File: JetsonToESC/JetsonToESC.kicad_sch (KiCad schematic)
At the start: 1 part, among them U1 ESP32-C3_SUPERMINI_TH

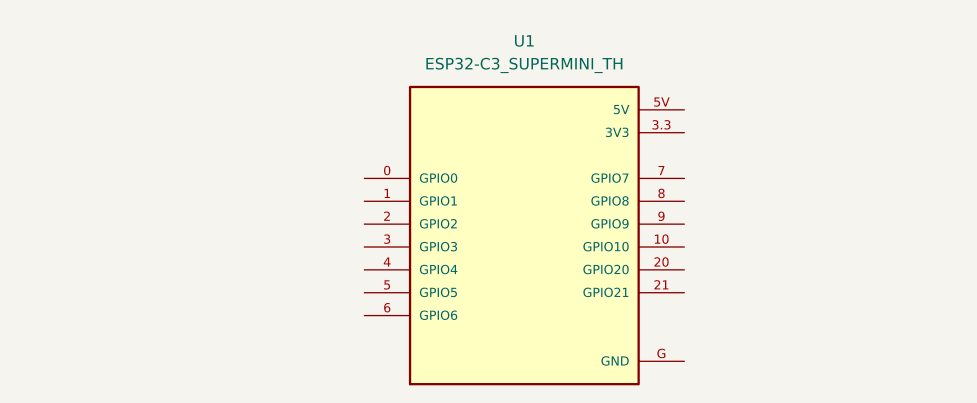
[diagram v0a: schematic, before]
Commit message: Added footprints, connectors and cutout
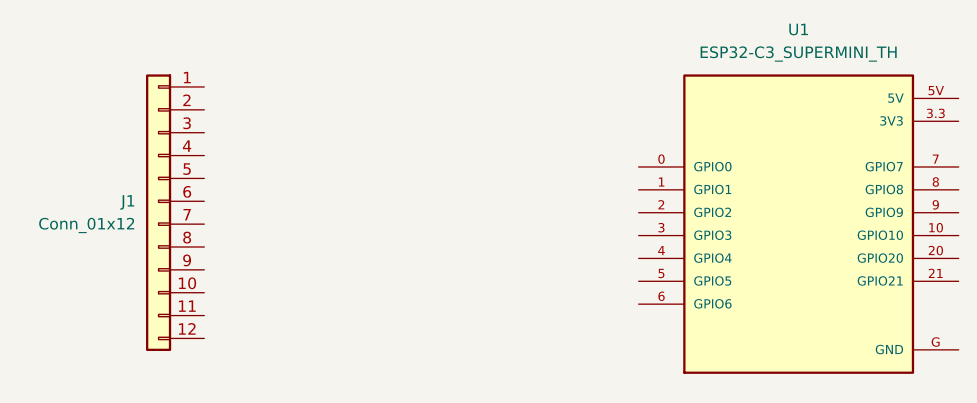
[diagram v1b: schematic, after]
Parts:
- added J1: Conn_01x12, Connector_PinSocket_2.54mm:PinSocket_1x12_P2.54mm_Horizontal, symbol Connector_Generic:Conn_01x12
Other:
- moved on the sheet: U1
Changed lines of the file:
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@@
 	(symbol
 		(lib_id "ESP32-C3_SUPERMINI_TH:ESP32-C3_SUPERMINI_TH")
-		(at 124.46 88.9 0)
+		(at 154.94 87.63 0)
 		(unit 1)
 		(exclude_from_sim no)
@@
 		(fields_autoplaced yes)
 		(property "Reference" "U1"
-			(at 124.46 68.58 0)
+			(at 154.94 67.31 0)
 			(effects
 				(font
@@
 		)
 		(property "Value" "ESP32-C3_SUPERMINI_TH"
-			(at 124.46 71.12 0)
+			(at 154.94 69.85 0)
 			(effects
 				(font
@@
 		)
 		(property "Footprint" "ESP32ModulesLibrary:MODULE_ESP32-C3_SUPERMINI_TH"
-			(at 124.46 88.9 0)
+			(at 154.94 87.63 0)
 			(effects
 				(font
@@
 		)
 		(property "Datasheet" ""
-			(at 124.46 88.9 0)
+			(at 154.94 87.63 0)
 			(effects
 				(font
@@
 		)
 		(property "Description" ""
-			(at 124.46 88.9 0)
+			(at 154.94 87.63 0)
 			(effects
 				(font
@@
 		)
 		(property "MF" "Espressif Systems"
-			(at 124.46 88.9 0)
+			(at 154.94 87.63 0)
 			(effects
 				(font
@@
 		)
 		(property "Description_1" "\n                        \n                            Super tiny ESP32-C3 board\n                        \n"
-			(at 124.46 88.9 0)
+			(at 154.94 87.63 0)
 			(effects
 				(font
@@
 		)
 		(property "CREATOR" "DIZAR"
-			(at 124.46 88.9 0)
+			(at 154.94 87.63 0)
 			(effects
 				(font
@@
 		)
 		(property "Price" "None"
-			(at 124.46 88.9 0)
+			(at 154.94 87.63 0)
 			(effects
 				(font
@@
 		)
 		(property "Package" "Package"
-			(at 124.46 88.9 0)
+			(at 154.94 87.63 0)
 			(effects
 				(font
@@
 		)
 		(property "Check_prices" "https://www.snapeda.com/parts/ESP32-C3%20SuperMini_TH/Espressif+Systems/view-part/?ref=eda"
-			(at 124.46 88.9 0)
+			(at 154.94 87.63 0)
 			(effects
 				(font
@@
 		)
 		(property "STANDARD" "IPC-7351B"
-			(at 124.46 88.9 0)
+			(at 154.94 87.63 0)
 			(effects
 				(font
@@
 		)
 		(property "VERIFIER" ""
-			(at 124.46 88.9 0)
+			(at 154.94 87.63 0)
 			(effects
 				(font
@@
 		)
 		(property "SnapEDA_Link" "https://www.snapeda.com/parts/ESP32-C3%20SuperMini_TH/Espressif+Systems/view-part/?ref=snap"
-			(at 124.46 88.9 0)
+			(at 154.94 87.63 0)
 			(effects
 				(font
@@
 		)
 		(property "MP" "ESP32-C3 SuperMini_TH"
-			(at 124.46 88.9 0)
+			(at 154.94 87.63 0)
 			(effects
 				(font
@@
 		)
 		(property "Availability" "Not in stock"
-			(at 124.46 88.9 0)
+			(at 154.94 87.63 0)
 			(effects
 				(font
@@
 		)
 		(property "MANUFACTURER" "Espressif Systems"
-			(at 124.46 88.9 0)
+			(at 154.94 87.63 0)
 			(effects
 				(font
@@
 					(unit 1)
 				)
+			)
+		)
+	)
+	(symbol
+		(lib_id "Connector_Generic:Conn_01x12")
+		(at 83.82 86.36 0)
+		(mirror y)
+		(unit 1)
+		(exclude_from_sim no)
+		(in_bom yes)
+		(on_board yes)
+		(dnp no)
+		(property "Reference" "J1"
+			(at 81.28 86.3599 0)
+			(effects
+				(font
+					(size 1.27 1.27)
+				)
+				(justify left)
+			)
+		)
+		(property "Value" "Conn_01x12"
+			(at 81.28 88.8999 0)
+			(effects
+				(font
+					(size 1.27 1.27)
+				)
+				(justify left)
+			)
+		)
+		(property "Footprint" "Connector_PinSocket_2.54mm:PinSocket_1x12_P2.54mm_Horizontal"
+			(at 83.82 86.36 0)
+			(effects
+				(font
+					(size 1.27 1.27)
+				)
+				(hide yes)
+			)
+		)
+		(property "Datasheet" "~"
+			(at 83.82 86.36 0)
+			(effects
+				(font
+					(size 1.27 1.27)
+				)
+				(hide yes)
+			)
+		)
+		(property "Description" "Generic connector, single row, 01x12, script generated (kicad-library-utils/schlib/autogen/connector/)"
+			(at 83.82 86.36 0)
+			(effects
+				(font
+					(size 1.27 1.27)
+				)
+				(hide yes)
+			)
+		)
+		(pin "10"
+		)
+		(pin "3"
+		)
+		(pin "1"
+		)
+		(pin "5"
+		)
+		(pin "12"
+		)
+		(pin "2"
+		)
+		(pin "7"
+		)
+		(pin "11"
+		)
+		(pin "4"
+		)
+		(pin "6"
+		)
+		(pin "9"
+		)
+		(pin "8"
+		)
+		(instances
+			(project ""
+				(path "/47af999a-55f7-4333-ac4c-b272b7fb2895"
+					(reference "J1")
+					(unit 1)
+				)

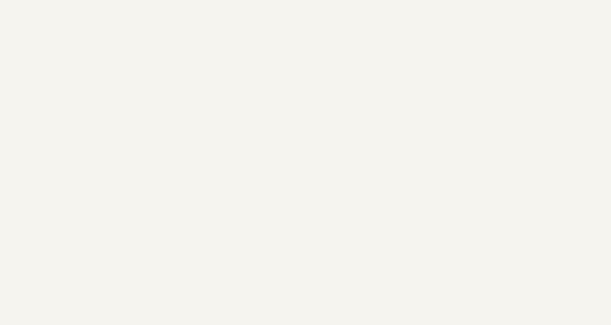
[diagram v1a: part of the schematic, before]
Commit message: Added mechanic drills
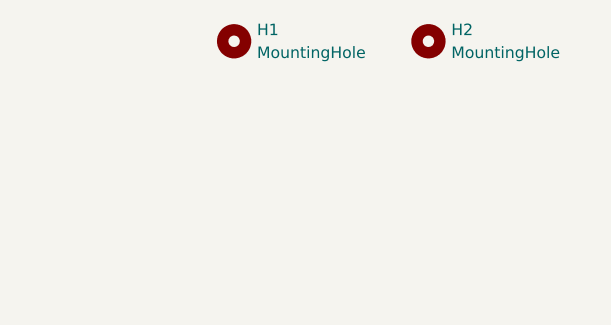
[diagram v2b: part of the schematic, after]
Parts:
- added H1, H2: MountingHole, TestPoint:TestPoint_Plated_Hole_D3.0mm, symbol Mechanical:MountingHole
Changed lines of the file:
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@@
 	(paper "A4")
+	(symbol
+		(lib_id "Mechanical:MountingHole")
+		(at 148.59 25.4 0)
+		(unit 1)
+		(exclude_from_sim yes)
+		(in_bom no)
+		(on_board yes)
+		(dnp no)
+		(fields_autoplaced yes)
+		(property "Reference" "H1"
+			(at 151.13 24.1299 0)
+			(effects
+				(font
+					(size 1.27 1.27)
+				)
+				(justify left)
+			)
+		)
+		(property "Value" "MountingHole"
+			(at 151.13 26.6699 0)
+			(effects
+				(font
+					(size 1.27 1.27)
+				)
+				(justify left)
+			)
+		)
+		(property "Footprint" "TestPoint:TestPoint_Plated_Hole_D3.0mm"
+			(at 148.59 25.4 0)
+			(effects
+				(font
+					(size 1.27 1.27)
+				)
+				(hide yes)
+			)
+		)
+		(property "Datasheet" "~"
+			(at 148.59 25.4 0)
+			(effects
+				(font
+					(size 1.27 1.27)
+				)
+				(hide yes)
+			)
+		)
+		(property "Description" "Mounting Hole without connection"
+			(at 148.59 25.4 0)
+			(effects
+				(font
+					(size 1.27 1.27)
+				)
+				(hide yes)
+			)
+		)
+		(instances
+			(project ""
+				(path "/47af999a-55f7-4333-ac4c-b272b7fb2895"
+					(reference "H1")
+					(unit 1)
+				)
+			)
+		)
+	)
 	(symbol
 		(lib_id "ESP32-C3_SUPERMINI_TH:ESP32-C3_SUPERMINI_TH")
@@
 					(unit 1)
 				)
+			)
+		)
+	)
+	(symbol
+		(lib_id "Mechanical:MountingHole")
+		(at 170.18 25.4 0)
+		(unit 1)
+		(exclude_from_sim yes)
+		(in_bom no)
+		(on_board yes)
+		(dnp no)
+		(fields_autoplaced yes)
+		(property "Reference" "H2"
+			(at 172.72 24.1299 0)
+			(effects
+				(font
+					(size 1.27 1.27)
+				)
+				(justify left)
+			)
+		)
+		(property "Value" "MountingHole"
+			(at 172.72 26.6699 0)
+			(effects
+				(font
+					(size 1.27 1.27)
+				)
+				(justify left)
+			)
+		)
+		(property "Footprint" "TestPoint:TestPoint_Plated_Hole_D3.0mm"
+			(at 170.18 25.4 0)
+			(effects
+				(font
+					(size 1.27 1.27)
+				)
+				(hide yes)
+			)
+		)
+		(property "Datasheet" "~"
+			(at 170.18 25.4 0)
+			(effects
+				(font
+					(size 1.27 1.27)
+				)
+				(hide yes)
+			)
+		)
+		(property "Description" "Mounting Hole without connection"
+			(at 170.18 25.4 0)
+			(effects
+				(font
+					(size 1.27 1.27)
+				)
+				(hide yes)
+			)
+		)
+		(instances
+			(project "JetsonToESC"
+				(path "/47af999a-55f7-4333-ac4c-b272b7fb2895"
+					(reference "H2")
+					(unit 1)
+				)

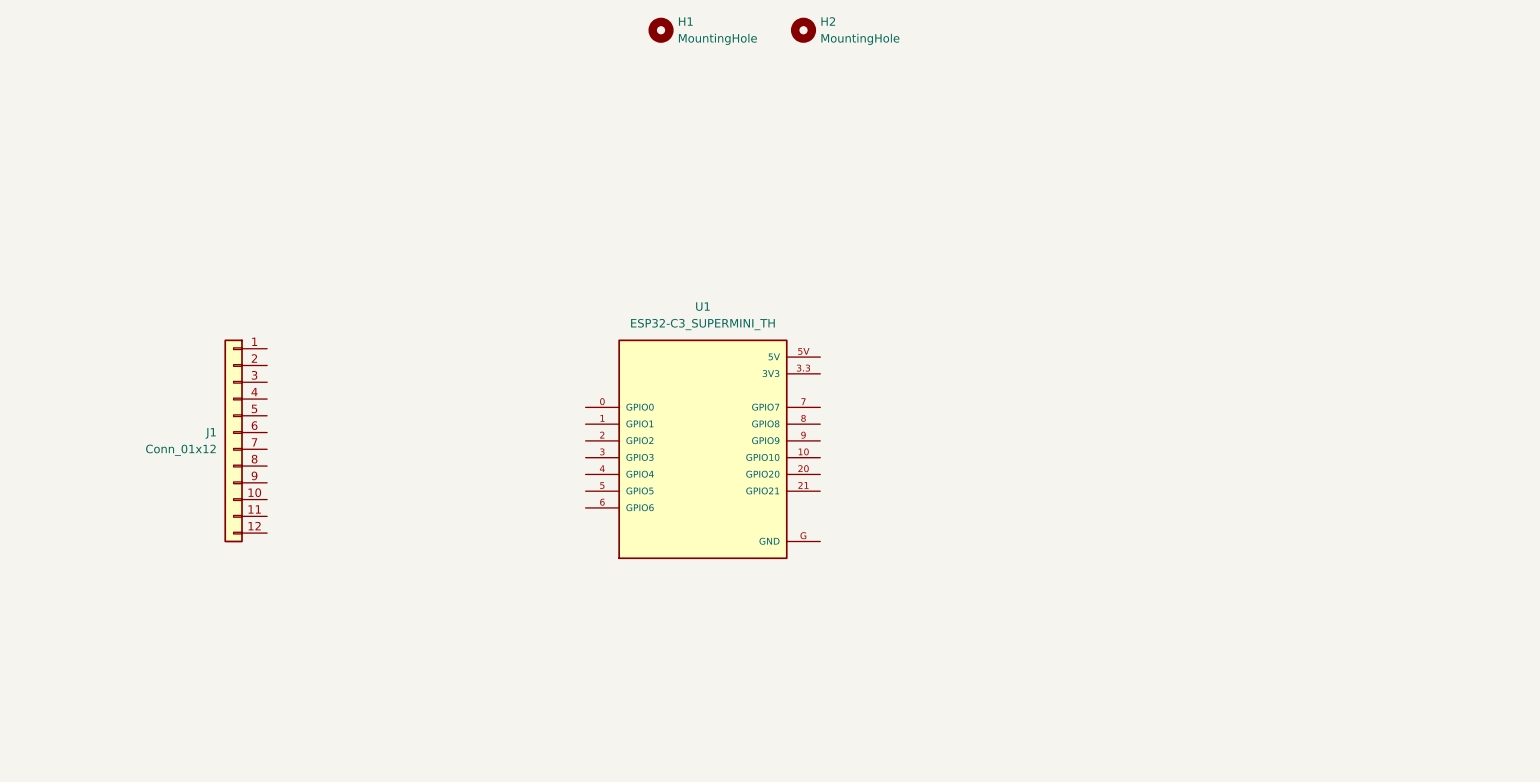
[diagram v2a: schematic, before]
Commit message: Added most of components and preliminar routing
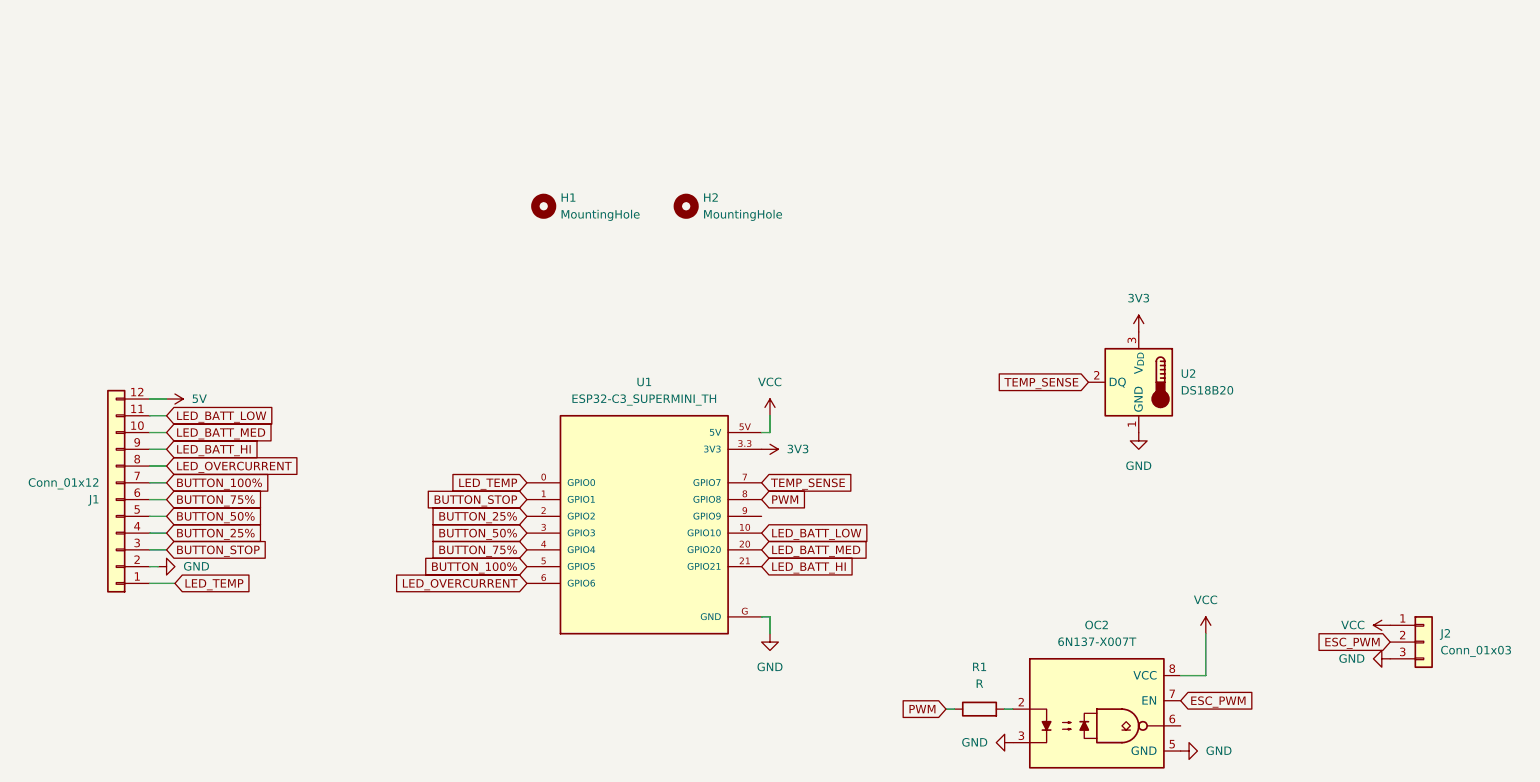
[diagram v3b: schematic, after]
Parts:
- added J2: Conn_01x03, Connector_JST:JST_EH_B3B-EH-A_1x03_P2.50mm_Vertical, symbol Connector_Generic:Conn_01x03
- added OC2: 6N137-X007T, PCM_Package_DIP_AKL:SMDIP-8_W9.53mm, symbol PCM_Optocoupler_Logic_AKL:6N137-X007T
- added R1: R, PCM_Resistor_SMD_AKL:R_0603_1608Metric, symbol Device:R
- added U2: DS18B20, Package_TO_SOT_THT:TO-92_Inline, symbol Sensor_Temperature:DS18B20
- H1, H2: footprint TestPoint:TestPoint_Plated_Hole_D3.0mm -> TestPoint:TestPoint_Plated_Hole_D2.0mm
- J1: footprint Connector_PinSocket_2.54mm:PinSocket_1x12_P2.54mm_Horizontal -> Connector_JST:JST_EH_S12B-EH_1x12_P2.50mm_Horizontal
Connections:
- net LED_TEMP: now reaches U1.0 (GPIO0)
- net LED_TEMP: now also J1.1 (Pin_1)
- net BUTTON_STOP: now reaches U1.1 (GPIO1)
- net BUTTON_STOP: now also J1.3 (Pin_3)
- net LED_BATT_LOW: now reaches U1.10 (GPIO10)
- net LED_BATT_LOW: now also J1.11 (Pin_11)
- net BUTTON_25%: now reaches U1.2 (GPIO2)
- net BUTTON_25%: now also J1.4 (Pin_4)
- net LED_BATT_MED: now reaches U1.20 (GPIO20)
- net LED_BATT_MED: now also J1.10 (Pin_10)
- net LED_BATT_HI: now reaches U1.21 (GPIO21)
- net LED_BATT_HI: now also J1.9 (Pin_9)
- net BUTTON_50%: now reaches U1.3 (GPIO3)
- net BUTTON_50%: now also J1.5 (Pin_5)
- net 3V3: now reaches U1.3.3 (3V3)
- net 3V3: now also U2.3 (V_{DD})
- net BUTTON_75%: now reaches U1.4 (GPIO4)
- net BUTTON_75%: now also J1.6 (Pin_6)
- net BUTTON_100%: now reaches U1.5 (GPIO5)
- net BUTTON_100%: now also J1.7 (Pin_7)
- net VCC: now reaches U1.5V
- net VCC: now also J2.1 (Pin_1), OC2.8 (VCC)
- net LED_OVERCURRENT: now reaches U1.6 (GPIO6)
- net LED_OVERCURRENT: now also J1.8 (Pin_8)
- net TEMP_SENSE: now reaches U1.7 (GPIO7)
- net TEMP_SENSE: now also U2.2 (DQ)
- net PWM: now reaches U1.8 (GPIO8)
- net PWM: now also R1.1
- net GND: now reaches U1.G (GND)
- net GND: now also J1.2 (Pin_2), J2.3 (Pin_3), OC2.3, OC2.5 (GND), U2.1 (GND)
- net 5V: now reaches J1.12 (Pin_12)
- new net: OC2.2, R1.2
- new net ESC_PWM: J2.2 (Pin_2), OC2.7 (EN)
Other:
- moved on the sheet: H1, H2, U1

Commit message: Design almost finished, added hierarchical sheets
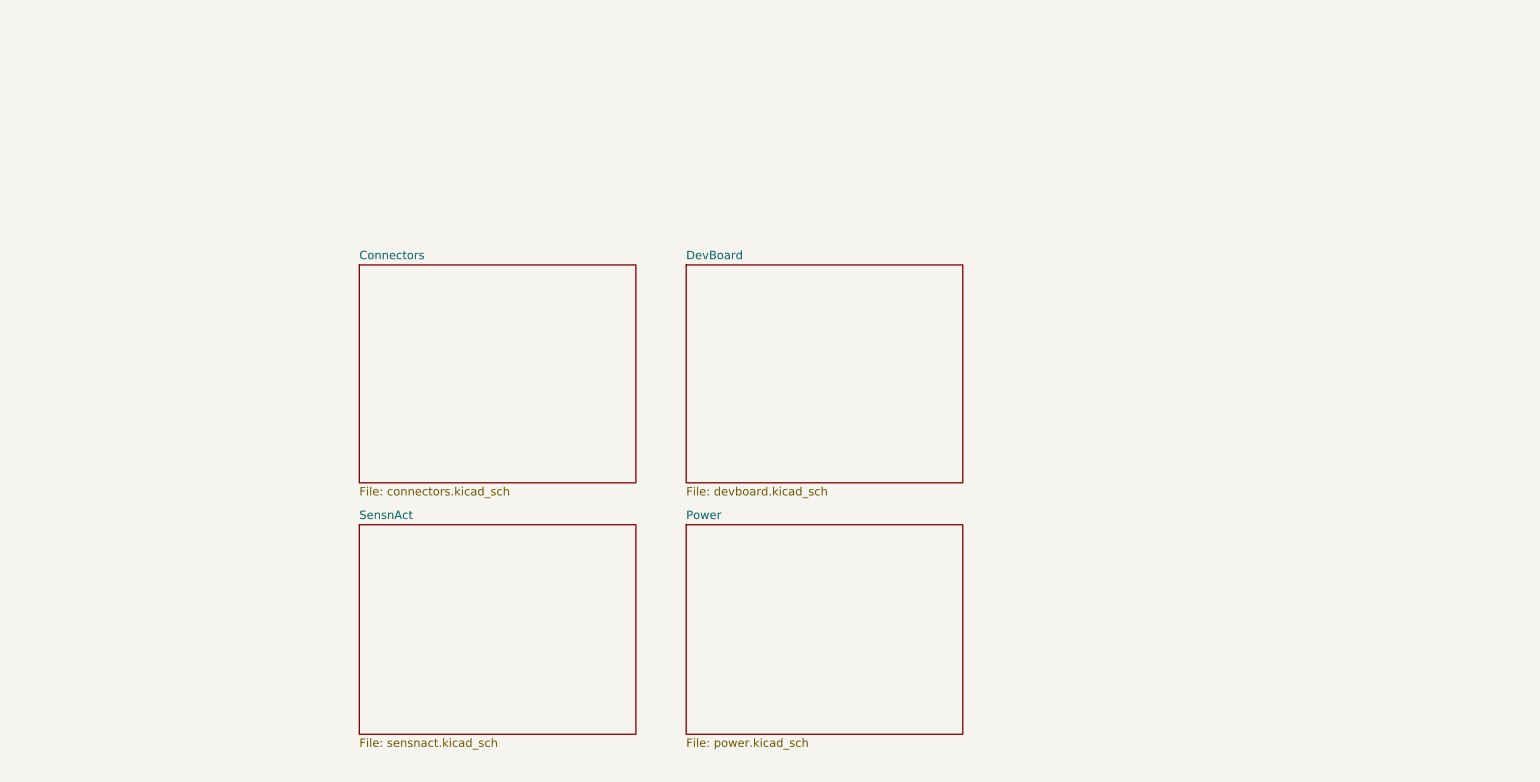
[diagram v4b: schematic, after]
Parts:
- removed H1, H2: MountingHole, TestPoint:TestPoint_Plated_Hole_D2.0mm, symbol Mechanical:MountingHole
- removed J1: Conn_01x12, Connector_JST:JST_EH_S12B-EH_1x12_P2.50mm_Horizontal, symbol Connector_Generic:Conn_01x12
- removed J2: Conn_01x03, Connector_JST:JST_EH_B3B-EH-A_1x03_P2.50mm_Vertical, symbol Connector_Generic:Conn_01x03
- removed OC2: 6N137-X007T, PCM_Package_DIP_AKL:SMDIP-8_W9.53mm, symbol PCM_Optocoupler_Logic_AKL:6N137-X007T
- removed R1: R, PCM_Resistor_SMD_AKL:R_0603_1608Metric, symbol Device:R
- removed U1: ESP32-C3_SUPERMINI_TH, ESP32ModulesLibrary:MODULE_ESP32-C3_SUPERMINI_TH, symbol ESP32-C3_SUPERMINI_TH:ESP32-C3_SUPERMINI_TH
- removed U2: DS18B20, Package_TO_SOT_THT:TO-92_Inline, symbol Sensor_Temperature:DS18B20
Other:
- added sheet Connectors (connectors.kicad_sch)
- added sheet DevBoard (devboard.kicad_sch)
- added sheet Power (power.kicad_sch)
- added sheet SensnAct (sensnact.kicad_sch)

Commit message: Start On this Branch
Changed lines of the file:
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@@
 	(generator "eeschema")
 	(generator_version "9.0")
-	(paper "A4")
+	(paper "A5")
 	(sheet
-		(at 102.87 100.33)
-		(size 41.91 31.75)
+		(at 106.68 63.5)
+		(size 41.91 33.02)
 		(exclude_from_sim no)
 		(in_bom yes)
 		(on_board yes)
 		(dnp no)
-		(fields_autoplaced yes)
 		(stroke
 			(width 0.1524)
@@
 		)
 		(property "Sheetname" "SensnAct"
-			(at 102.87 99.6184 0)
+			(at 115.824 82.042 0)
 			(effects
 				(font
-					(size 1.27 1.27)
+					(size 3 3)
+					(thickness 0.6)
+					(bold yes)
 				)
 				(justify left bottom)
@@
 		)
 		(property "Sheetfile" "sensnact.kicad_sch"
-			(at 102.87 132.6646 0)
+			(at 106.68 95.8346 0)
 			(effects
 				(font
@@
 				)
 				(justify left top)
+				(hide yes)
 			)
 		)
@@
 	)
 	(sheet
-		(at 152.4 60.96)
-		(size 41.91 33.02)
+		(at 106.68 26.67)
+		(size 41.91 31.75)
 		(exclude_from_sim no)
 		(in_bom yes)
 		(on_board yes)
 		(dnp no)
-		(fields_autoplaced yes)
 		(stroke
 			(width 0.1524)
@@
 		)
 		(property "Sheetname" "DevBoard"
-			(at 152.4 60.2484 0)
+			(at 115.824 45.212 0)
 			(effects
 				(font
-					(size 1.27 1.27)
+					(size 3 3)
+					(thickness 0.6)
+					(bold yes)
 				)
 				(justify left bottom)
@@
 		)
 		(property "Sheetfile" "devboard.kicad_sch"
-			(at 152.4 94.5646 0)
+			(at 106.68 60.2746 0)
 			(effects
 				(font
@@
 				)
 				(justify left top)
+				(hide yes)
 			)
 		)
@@
 	)
 	(sheet
-		(at 152.4 100.33)
+		(at 57.15 26.67)
 		(size 41.91 31.75)
 		(exclude_from_sim no)
@@
 		(on_board yes)
 		(dnp no)
-		(fields_autoplaced yes)
 		(stroke
 			(width 0.1524)
@@
 		)
 		(property "Sheetname" "Power"
-			(at 152.4 99.6184 0)
+			(at 70.358 44.704 0)
 			(effects
 				(font
-					(size 1.27 1.27)
+					(size 3 3)
+					(thickness 0.6)
+					(bold yes)
 				)
 				(justify left bottom)
@@
 		)
 		(property "Sheetfile" "power.kicad_sch"
-			(at 152.4 132.6646 0)
+			(at 57.15 59.0046 0)
 			(effects
 				(font
@@
 				)
 				(justify left top)
+				(hide yes)
 			)
 		)
@@
 	)
 	(sheet
-		(at 102.87 60.96)
+		(at 57.15 63.5)
 		(size 41.91 33.02)
 		(exclude_from_sim no)
@@
 		(on_board yes)
 		(dnp no)
-		(fields_autoplaced yes)
 		(stroke
 			(width 0.1524)
@@
 		)
 		(property "Sheetname" "Connectors"
-			(at 102.87 60.2484 0)
+			(at 65.532 82.296 0)
 			(effects
 				(font
-					(size 1.27 1.27)
+					(size 3 3)
+					(thickness 0.6)
+					(bold yes)
 				)
 				(justify left bottom)
@@
 		)
 		(property "Sheetfile" "connectors.kicad_sch"
-			(at 102.87 94.5646 0)
+			(at 57.15 97.1046 0)
 			(effects
 				(font
@@
 				)
 				(justify left top)
+				(hide yes)
 			)
 		)
